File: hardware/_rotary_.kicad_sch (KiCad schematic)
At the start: 16 parts, among them J1 mono_jack_3.5mm, J2 jst_xa_3, U1 TLV2372, U2 LM317

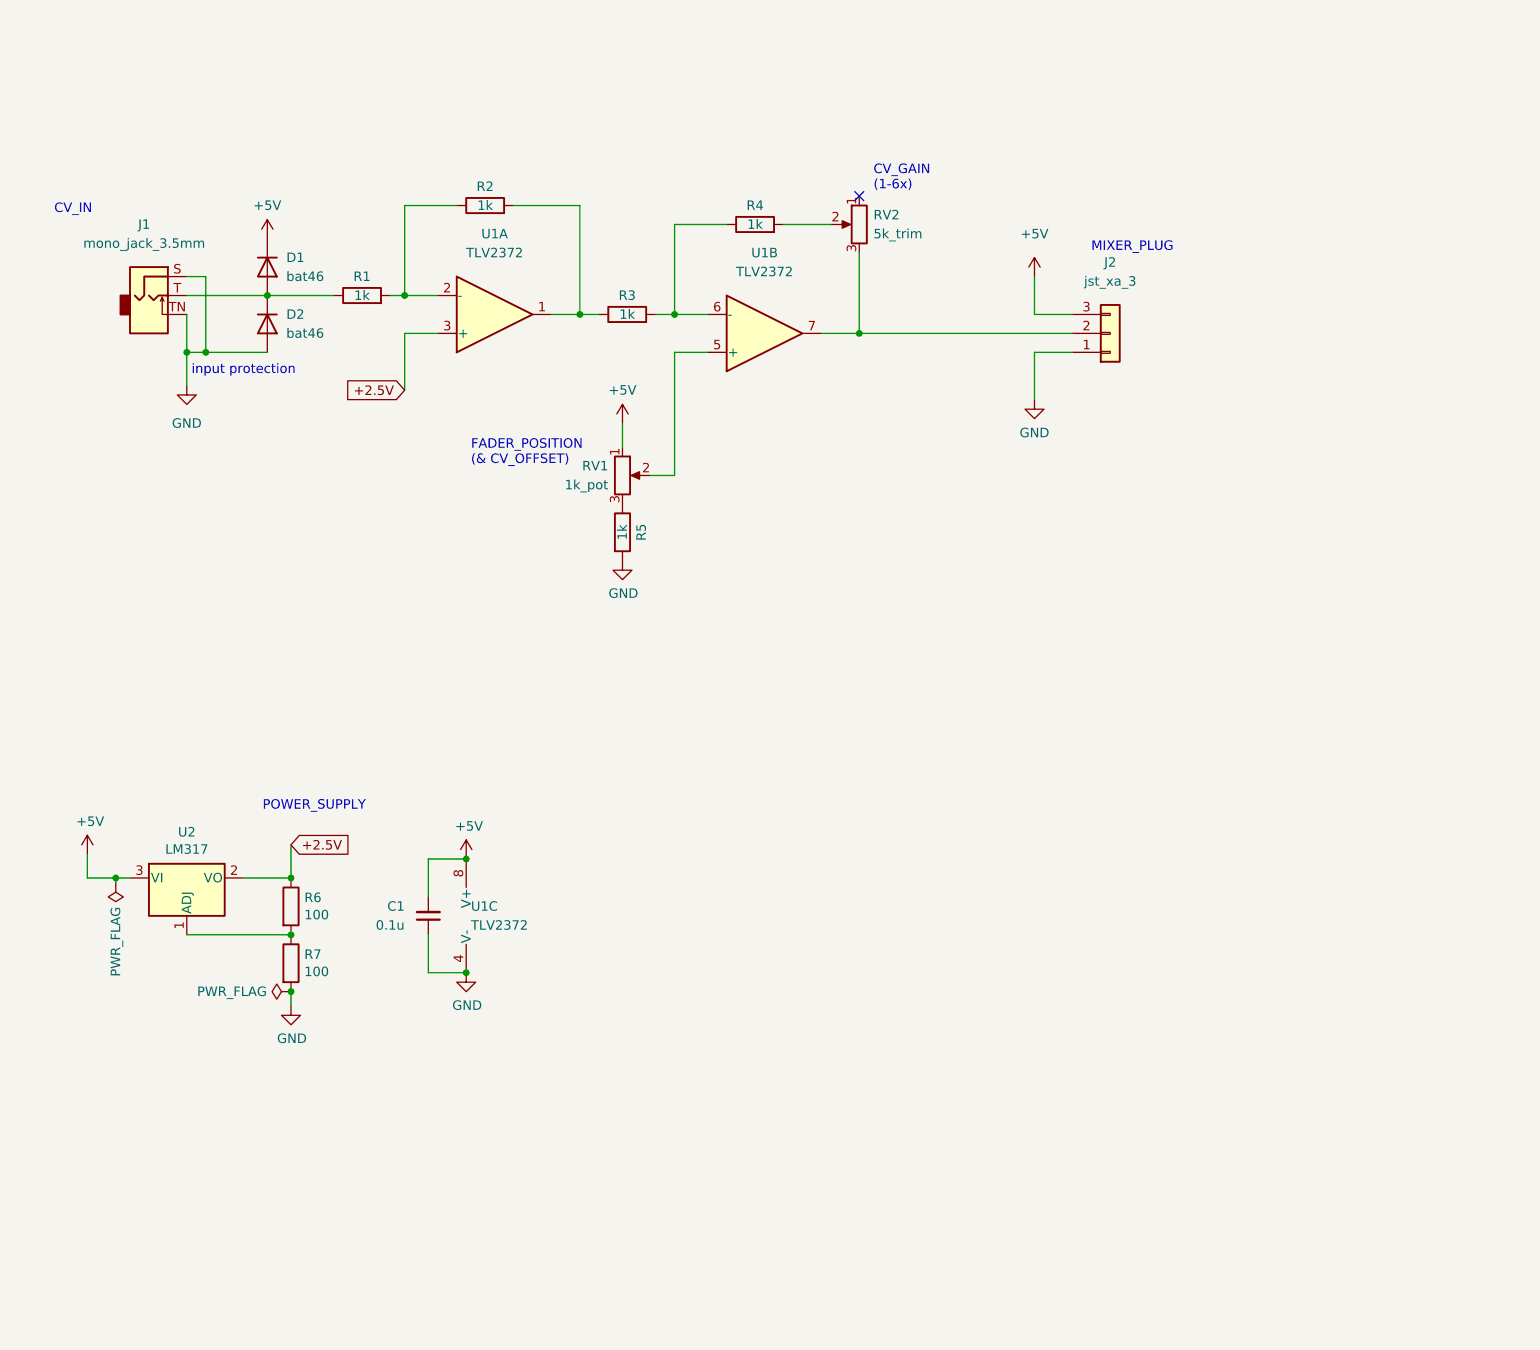
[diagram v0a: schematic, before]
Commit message: updated circuit and panel to include envelope follower
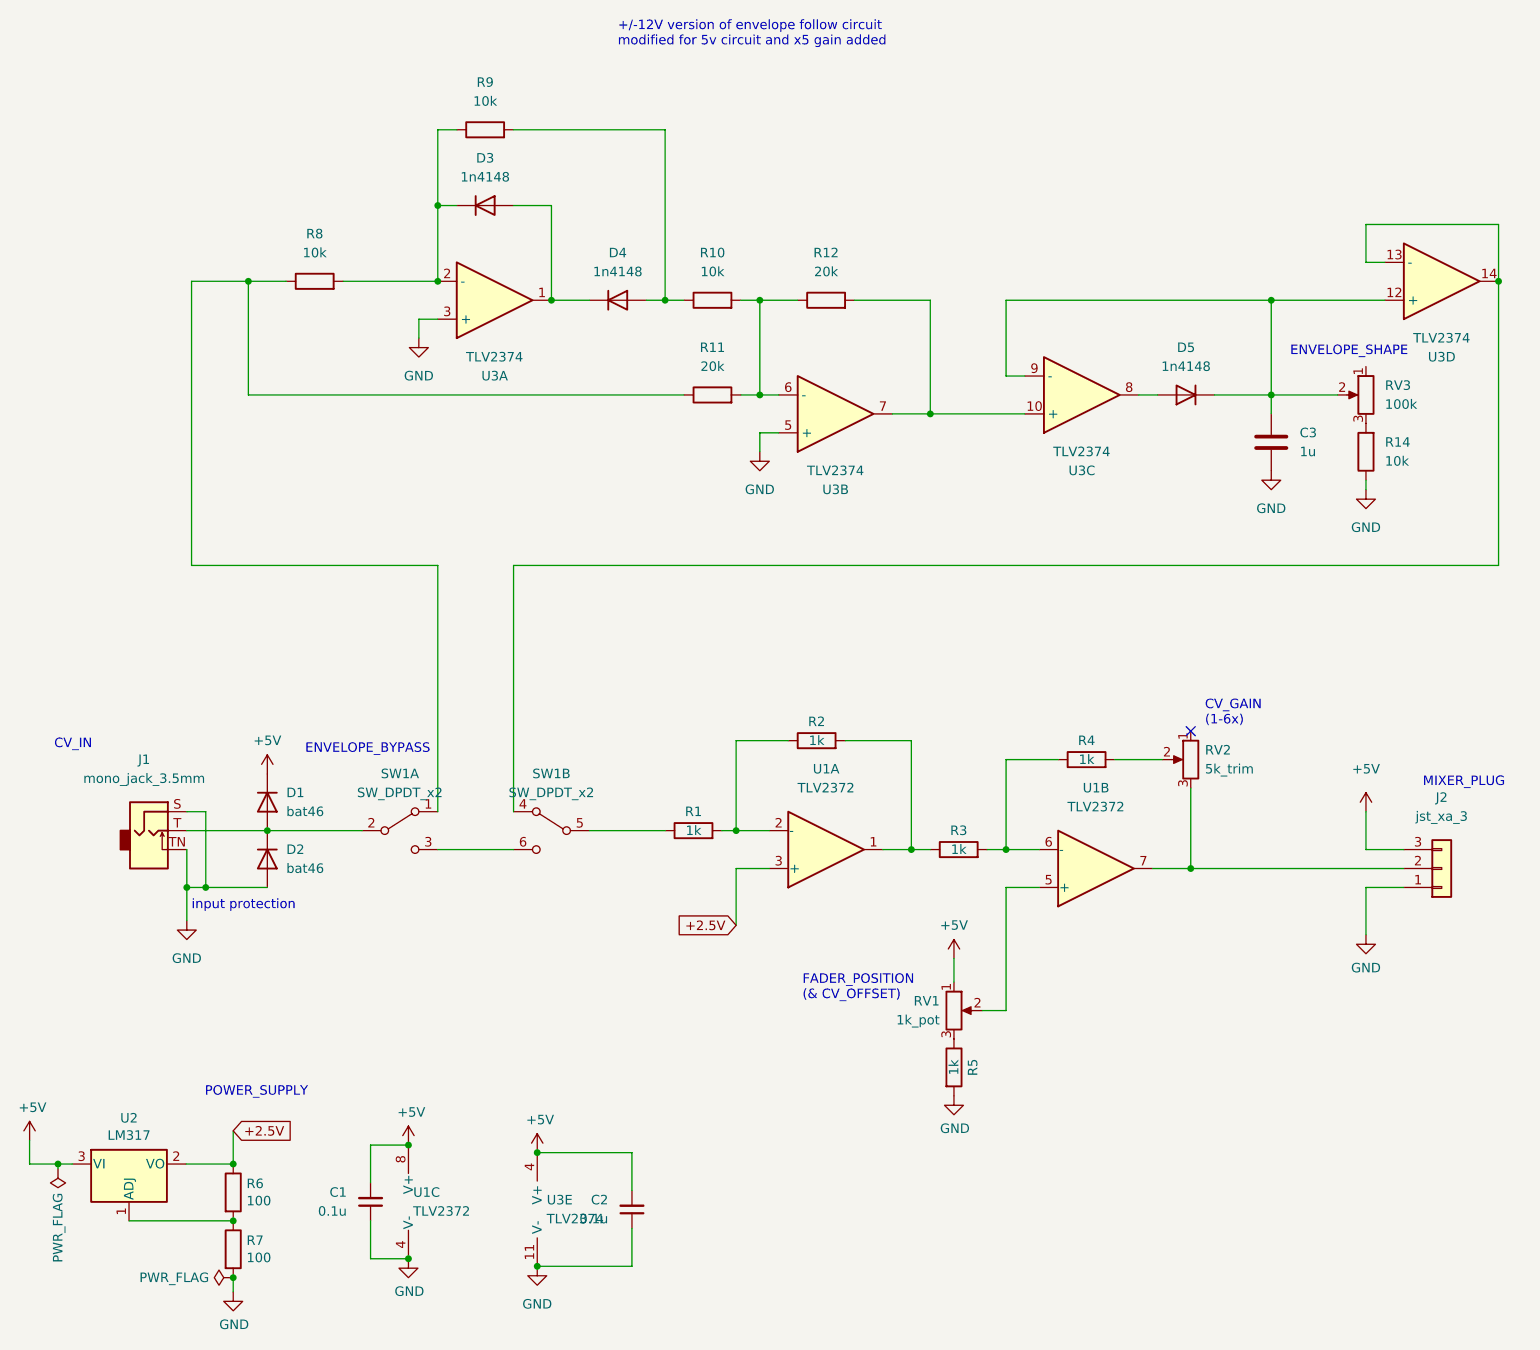
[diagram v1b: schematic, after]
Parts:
- added C2: 0.1u, Capacitor_THT:C_Disc_D7.0mm_W2.5mm_P5.00mm, symbol Device:C_Small
- added C3: 1u, Capacitor_THT:C_Disc_D7.0mm_W2.5mm_P5.00mm, symbol Device:C
- added D3, D4, D5: 1n4148, Diode_THT:D_DO-34_SOD68_P7.62mm_Horizontal, symbol Device:D
- added R10, R14, R8, R9: 10k, Resistor_THT:R_Axial_DIN0207_L6.3mm_D2.5mm_P7.62mm_Horizontal, symbol Device:R
- added R11, R12: 20k, Resistor_THT:R_Axial_DIN0207_L6.3mm_D2.5mm_P7.62mm_Horizontal, symbol Device:R
- added RV3: 100k, lib_fp:Potentiometer_Vertical_Large, symbol Device:R_Potentiometer
- added SW1: SW_DPDT_x2, lib_fp:dpdt_mini_toggle_switch_tayda, symbol Switch:SW_DPDT_x2
- added U3: TLV2374, Package_DIP:DIP-14_W7.62mm_LongPads, symbol Device:Opamp_Quad
- RV2: footprint lib_fp:tht_vertical_trim_3362 -> lib_fp:Potentiometer_Vertical_Large
- U1: footprint lib_fp:DIP-SOIC-8 -> Package_DIP:DIP-8_W7.62mm_LongPads
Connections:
- net +5V: now also C2.2, U3.4 (V+)
- net GND: now also C2.1, C3.2, R14.1, U3.11 (V-), U3.3 (+), U3.5 (+)
- net at D1.2 (A), D2.1 (K), J1.T: now also SW1.2 (B); no longer R1.1
- new net: C3.1, D5.1 (K), RV3.2, U3.12 (+), U3.9 (-)
- new net: D5.2 (A), U3.8
- new net: R11.1, R8.1, SW1.1 (A)
- new net: D3.1 (K), R8.2, R9.1, U3.2 (-)
- new net: R1.1, SW1.5 (B)
- new net: D3.2 (A), D4.1 (K), U3.1
- new net: SW1.3 (C), SW1.6 (C)
- new net: R10.2, R11.2, R12.1, U3.6 (-)
- new net: R12.2, U3.10 (+), U3.7
- new net: D4.2 (A), R10.1, R9.2
- new net: R14.2, RV3.3
- new net: SW1.4 (A), U3.13 (-), U3.14
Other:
- note added: "+/-12V version of envelope follow circuit modified for 5v circuit and x5 gain added"
- note added: "ENVELOPE_BYPASS"
- note added: "ENVELOPE_SHAPE"
- moved on the sheet: C1, D1, D2, J1, J2, R1, R2, R3, R4, R5, R6, R7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

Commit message: preparing v1_1_0 for release
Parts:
- added R13: 2.4k, Resistor_THT:R_Axial_DIN0207_L6.3mm_D2.5mm_P7.62mm_Horizontal, symbol Device:R
- added R15: 1k, Resistor_THT:R_Axial_DIN0207_L6.3mm_D2.5mm_P7.62mm_Horizontal, symbol Device:R
- RV2: value 5k_trim -> 5k_pot
- RV3: value 100k -> 100k_pot
- U2: footprint Package_TO_SOT_THT:TO-92_Inline -> Package_TO_SOT_THT:TO-92_HandSolder
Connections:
- net GND: now also R15.2
- net at R11.1, R8.1: now also SW1.3 (C); no longer SW1.1 (A)
- net at SW1.6 (C): now also U3.14, R13.1; no longer SW1.3 (C)
- new net: SW1.1 (A), SW1.4 (A)
- new net: R13.2, R15.1, U3.13 (-)
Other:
- company: cyberboy666 -> cyberboy666 & autr
- moved on the sheet: SW1B
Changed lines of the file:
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@@
   (title_block
     (title "_rotary_")
-    (date "2022-11-24")
-    (rev "v0_1_0")
-    (company "cyberboy666")
+    (date "2024-09-18")
+    (rev "v1_1_0")
+    (company "cyberboy666 & autr")
   )
   (junction (at 45.085 132.08) (diameter 0) (color 0 0 0 0)
@@
   )
   (junction (at 53.34 50.8) (diameter 0) (color 0 0 0 0)
+  )
+  (junction (at 203.2 43.18) (diameter 0) (color 0 0 0 0)
   )
   (junction (at 92.075 167.64) (diameter 0) (color 0 0 0 0)
@@
     (stroke (width 0) (type default))
   )
+  (wire (pts (xy 198.12 43.18) (xy 203.2 43.18))
+    (stroke (width 0) (type default))
+  )
   (wire (pts (xy 144.78 68.58) (xy 157.48 68.58))
     (stroke (width 0) (type default))
@@
     (stroke (width 0) (type default))
   )
-  (wire (pts (xy 203.2 43.18) (xy 220.98 43.18))
+  (wire (pts (xy 203.2 43.18) (xy 208.28 43.18))
     (stroke (width 0) (type default))
   )
@@
     (stroke (width 0) (type default))
   )
+  (wire (pts (xy 215.9 43.18) (xy 220.98 43.18))
+    (stroke (width 0) (type default))
+  )
   (wire (pts (xy 190.5 53.34) (xy 205.74 53.34))
     (stroke (width 0) (type default))
@@
   )
   (wire (pts (xy 88.9 30.48) (xy 109.22 30.48))
+    (stroke (width 0) (type default))
+  )
+  (wire (pts (xy 190.5 43.18) (xy 190.5 45.72))
     (stroke (width 0) (type default))
   )
@@
       (effects (font (size 1.27 1.27)))
     )
-    (property "Footprint" "Package_TO_SOT_THT:TO-92_Inline" (at 37.338 163.449 0)
+    (property "Footprint" "Package_TO_SOT_THT:TO-92_HandSolder" (at 37.338 163.449 0)
       (effects (font (size 1.27 1.27) italic) hide)
     )
@@
       (effects (font (size 1.27 1.27)) (justify right))
     )
-    (property "Value" "5k_trim" (at 181.61 116.2049 0)
+    (property "Value" "5k_pot" (at 181.61 116.2049 0)
       (effects (font (size 1.27 1.27)) (justify right))
     )
@@
     )
   )
-  (symbol (lib_id "Switch:SW_DPDT_x2") (at 73.66 124.46 0) (unit 1)
-    (in_bom yes) (on_board yes) (dnp no) (fields_autoplaced)
-    (property "Reference" "SW1" (at 73.66 116.84 0)
-      (effects (font (size 1.27 1.27)))
-    )
-    (property "Value" "SW_DPDT_x2" (at 73.66 119.38 0)
+  (symbol (lib_id "Switch:SW_DPDT_x2") (at 73.66 124.46 0) (mirror x) (unit 1)
+    (in_bom yes) (on_board yes) (dnp no)
+    (property "Reference" "SW1" (at 73.66 132.08 0)
+      (effects (font (size 1.27 1.27)))
+    )
+    (property "Value" "SW_DPDT_x2" (at 73.66 129.54 0)
       (effects (font (size 1.27 1.27)))
     )
@@
     )
   )
+  (symbol (lib_id "Device:R") (at 212.09 43.18 270) (unit 1)
+    (in_bom yes) (on_board yes) (dnp no) (fields_autoplaced)
+    (property "Reference" "R13" (at 212.09 36.83 90)
+      (effects (font (size 1.27 1.27)))
+    )
+    (property "Value" "2.4k" (at 212.09 39.37 90)
+      (effects (font (size 1.27 1.27)))
+    )
+    (property "Footprint" "Resistor_THT:R_Axial_DIN0207_L6.3mm_D2.5mm_P7.62mm_Horizontal" (at 212.09 41.402 90)
+      (effects (font (size 1.27 1.27)) hide)
+    )
+    (property "Datasheet" "~" (at 212.09 43.18 0)
+      (effects (font (size 1.27 1.27)) hide)
+    )
+    (pin "1")
+    (pin "2")
+    (instances
+      (project "_rotary_"
+        (path "/3cbd8b52-36f0-4c37-958a-5a88161dcf31"
+          (reference "R13") (unit 1)
+        )
+      )
+      (project "envelope_follow_test"
+        (path "/d55b0867-1c5b-42ac-8269-e89ebbd103e4"
+          (reference "R6") (unit 1)
+        )
+      )
+    )
+  )
   (symbol (lib_id "Device:R") (at 130.81 53.34 90) (unit 1)
     (in_bom yes) (on_board yes) (dnp no) (fields_autoplaced)
@@
     )
   )
-  (symbol (lib_id "Switch:SW_DPDT_x2") (at 93.98 124.46 0) (mirror y) (unit 2)
-    (in_bom yes) (on_board yes) (dnp no) (fields_autoplaced)
-    (property "Reference" "SW1" (at 93.98 116.84 0)
-      (effects (font (size 1.27 1.27)))
-    )
-    (property "Value" "SW_DPDT_x2" (at 93.98 119.38 0)
+  (symbol (lib_id "Switch:SW_DPDT_x2") (at 93.98 124.46 180) (unit 2)
+    (in_bom yes) (on_board yes) (dnp no)
+    (property "Reference" "SW1" (at 93.98 132.08 0)
+      (effects (font (size 1.27 1.27)))
+    )
+    (property "Value" "SW_DPDT_x2" (at 93.98 129.54 0)
       (effects (font (size 1.27 1.27)))
     )
@@
       (effects (font (size 1.27 1.27)) (justify right))
     )
-    (property "Value" "100k" (at 205.74 67.31 0)
+    (property "Value" "100k_pot" (at 205.74 67.31 0)
       (effects (font (size 1.27 1.27)) (justify right))
     )
@@
         (path "/3cbd8b52-36f0-4c37-958a-5a88161dcf31"
           (reference "#PWR05") (unit 1)
+        )
+      )
+    )
+  )
+  (symbol (lib_id "power:GND") (at 190.5 45.72 0) (unit 1)
+    (in_bom yes) (on_board yes) (dnp no) (fields_autoplaced)
+    (property "Reference" "#PWR09" (at 190.5 52.07 0)
+      (effects (font (size 1.27 1.27)) hide)
+    )
+    (property "Value" "GND" (at 190.5 50.8 0)
+      (effects (font (size 1.27 1.27)))
+    )
+    (property "Footprint" "" (at 190.5 45.72 0)
+      (effects (font (size 1.27 1.27)) hide)
+    )
+    (property "Datasheet" "" (at 190.5 45.72 0)
+      (effects (font (size 1.27 1.27)) hide)
+    )
+    (pin "1")
+    (instances
+      (project "_rotary_"
+        (path "/3cbd8b52-36f0-4c37-958a-5a88161dcf31"
+          (reference "#PWR09") (unit 1)
+        )
+      )
+      (project "envelope_follow_test"
+        (path "/d55b0867-1c5b-42ac-8269-e89ebbd103e4"
+          (reference "#PWR01") (unit 1)
         )
       )
@@
         )
       )
+    )
+  )
+  (symbol (lib_id "Device:R") (at 194.31 43.18 270) (unit 1)
+    (in_bom yes) (on_board yes) (dnp no) (fields_autoplaced)
+    (property "Reference" "R15" (at 194.31 36.83 90)
+      (effects (font (size 1.27 1.27)))
+    )
+    (property "Value" "1k" (at 194.31 39.37 90)
+      (effects (font (size 1.27 1.27)))
+    )
+    (property "Footprint" "Resistor_THT:R_Axial_DIN0207_L6.3mm_D2.5mm_P7.62mm_Horizontal" (at 194.31 41.402 90)
+      (effects (font (size 1.27 1.27)) hide)
+    )
+    (property "Datasheet" "~" (at 194.31 43.18 0)
+      (effects (font (size 1.27 1.27)) hide)
+    )
+    (pin "1")
+    (pin "2")
+    (instances
+      (project "_rotary_"
+        (path "/3cbd8b52-36f0-4c37-958a-5a88161dcf31"
+          (reference "R15") (unit 1)
+        )
+      )
+      (project "envelope_follow_test"
+        (path "/d55b0867-1c5b-42ac-8269-e89ebbd103e4"
+          (reference "R6") (unit 1)
+        )
+      )

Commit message: update pcbs and panels
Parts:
- RV1: value 1k_pot -> 1k_pot_d
